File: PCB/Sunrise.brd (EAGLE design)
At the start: 73 x 44 mm, 66 parts, among them IC1 STNS01, IC2 MT2492, J2 B2B-PH-K-S, J3 POWER_JACK, M1 E73-2G4M04S, Q1 IRLHM630, Q2 IRLHM630, Q3 IRLHM630

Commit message: PCB: Clean schematic, move values on board around a bit, no actual connectivity or component changes
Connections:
- new net SLEEP: M1.29
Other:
- board text added: "+ G R B"
- board text removed: "+ R G B"

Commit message: PCB: Minor update to NRF52 module; specify a package variant and expand its description
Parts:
- M1: value E73-2G4M04S -> E73-2G4M04S1B
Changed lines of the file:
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@@
 <attribute name="VALUE" x="26" y="18.5" size="0.6" layer="27" font="vector" ratio="15" rot="R180" align="center"/>
 </element>
-<element name="M1" library="E73-2G4M04S" package="E73-2GM404S" value="E73-2G4M04S" x="64.28" y="29.48" smashed="yes">
+<element name="M1" library="E73-2G4M04S" package="E73-2GM404S" value="E73-2G4M04S1B" x="64.28" y="29.48" smashed="yes">
 <attribute name="NAME" x="71.03" y="39.98" size="0.6" layer="25" font="vector" ratio="15" align="center"/>
 <attribute name="VALUE" x="64.28" y="29.48" size="0.6" layer="27" font="vector" ratio="15" align="center"/>

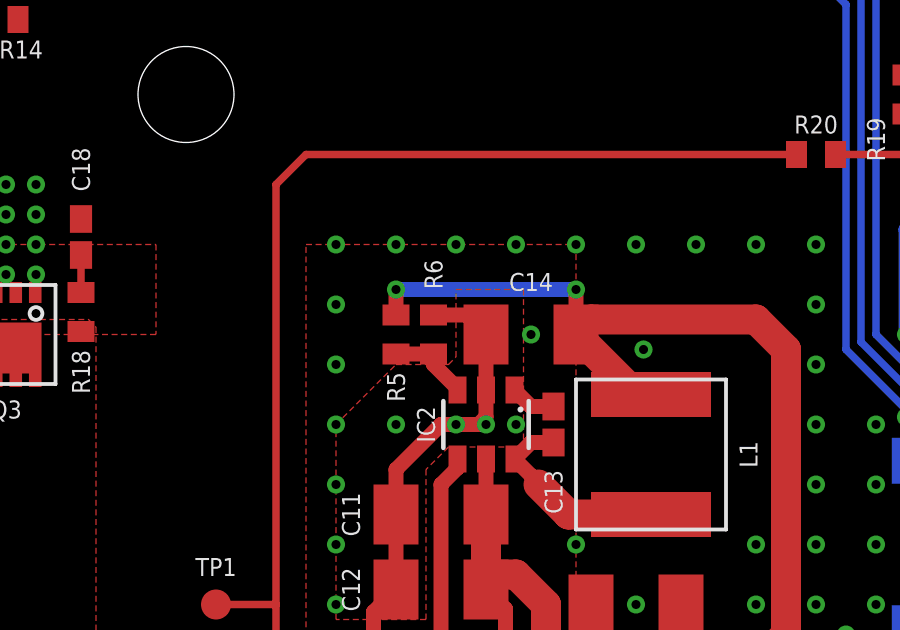
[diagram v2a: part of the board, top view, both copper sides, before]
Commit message: Relabel red/green/blue channels to match common RGB strips
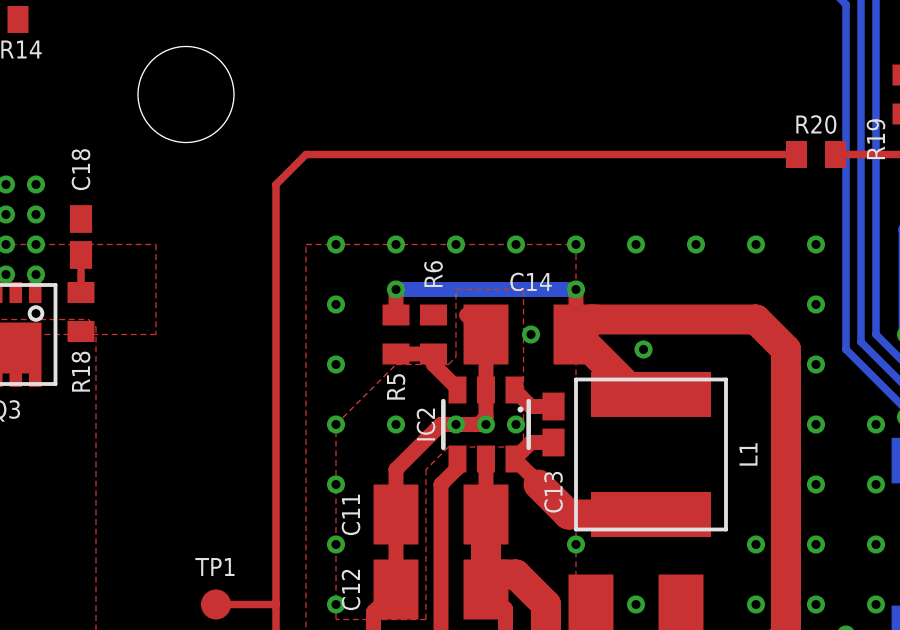
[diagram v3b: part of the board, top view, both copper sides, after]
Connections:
- net BG: now also M1.26, Q3.GATE, R14.2, TP5.TP; no longer M1.28, Q1.GATE, R12.2, TP3.TP
- net GG: now also M1.28, Q1.GATE, R12.2, TP3.TP; no longer M1.27, Q2.GATE, R13.2, TP4.TP
- net RG: now also M1.27, Q2.GATE, R13.2, TP4.TP; no longer M1.26, Q3.GATE, R14.2, TP5.TP
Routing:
- net BG: track 79.9 -> 65.0 mm
- net GG: track 71.5 -> 79.9 mm
- net RG: track 65.0 -> 71.5 mm
- net GND: track 14.8 -> 13.7 mm
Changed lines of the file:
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@@
 <setting verticaltext="up"/>
 </settings>
-<grid distance="0.25" unitdist="mm" unit="mm" style="lines" multiple="8" display="no" altdistance="0.025" altunitdist="inch" altunit="inch"/>
+<grid distance="0.25" unitdist="mm" unit="mm" style="lines" multiple="4" display="yes" altdistance="0.025" altunitdist="inch" altunit="inch"/>
 <layers>
 <layer number="1" name="Top" color="4" fill="1" visible="yes" active="yes"/>
@@
 <layer number="20" name="Dimension" color="15" fill="1" visible="yes" active="yes"/>
 <layer number="21" name="tPlace" color="7" fill="1" visible="yes" active="yes"/>
-<layer number="22" name="bPlace" color="7" fill="1" visible="no" active="yes"/>
+<layer number="22" name="bPlace" color="7" fill="1" visible="yes" active="yes"/>
 <layer number="23" name="tOrigins" color="15" fill="1" visible="yes" active="yes"/>
-<layer number="24" name="bOrigins" color="15" fill="1" visible="no" active="yes"/>
+<layer number="24" name="bOrigins" color="15" fill="1" visible="yes" active="yes"/>
 <layer number="25" name="tNames" color="7" fill="1" visible="yes" active="yes"/>
-<layer number="26" name="bNames" color="7" fill="1" visible="no" active="yes"/>
-<layer number="27" name="tValues" color="10" fill="1" visible="no" active="yes"/>
+<layer number="26" name="bNames" color="7" fill="1" visible="yes" active="yes"/>
+<layer number="27" name="tValues" color="23" fill="1" visible="no" active="yes"/>
 <layer number="28" name="bValues" color="7" fill="1" visible="no" active="yes"/>
 <layer number="29" name="tStop" color="7" fill="3" visible="yes" active="yes"/>
-<layer number="30" name="bStop" color="7" fill="6" visible="no" active="yes"/>
+<layer number="30" name="bStop" color="7" fill="6" visible="yes" active="yes"/>
 <layer number="31" name="tCream" color="7" fill="4" visible="no" active="yes"/>
 <layer number="32" name="bCream" color="7" fill="5" visible="no" active="yes"/>
@@
 <layer number="50" name="dxf" color="7" fill="1" visible="no" active="no"/>
 <layer number="51" name="tDocu" color="7" fill="1" visible="yes" active="yes"/>
-<layer number="52" name="bDocu" color="7" fill="1" visible="no" active="yes"/>
+<layer number="52" name="bDocu" color="7" fill="1" visible="yes" active="yes"/>
 <layer number="53" name="tGND_GNDA" color="7" fill="9" visible="no" active="no"/>
 <layer number="54" name="bGND_GNDA" color="1" fill="9" visible="no" active="no"/>
@@
 <contactref element="R9" pad="1"/>
 <wire x1="29" y1="27.15" x2="29" y2="29" width="0.5" layer="1"/>
-<wire x1="27.25" y1="29.65" x2="28.35" y2="29.65" width="0.5" layer="1"/>
 <wire x1="28.35" y1="29.65" x2="29" y2="29" width="0.5" layer="1"/>
 <wire x1="26" y1="20.5" x2="26" y2="23" width="0.5" layer="1"/>
@@
 <vertex x="48" y="16"/>
 </polygon>
-<polygon width="0.25" layer="1" spacing="0.2" thermals="no" rank="6">
+<polygon width="0.25" layer="1" spacing="0.2" rank="6">
 <vertex x="32" y="32"/>
 <vertex x="32" y="17"/>
@@
 <wire x1="32.65" y1="19.85" x2="32.5" y2="20" width="0.5" layer="1"/>
 </signal>
-<signal name="RG">
+<signal name="BG">
 <contactref element="M1" pad="26"/>
 <contactref element="Q3" pad="GATE"/>
@@
 <contactref element="TP5" pad="TP"/>
 </signal>
-<signal name="GG">
+<signal name="RG">
 <contactref element="M1" pad="27"/>
 <contactref element="Q2" pad="GATE"/>
@@
 <contactref element="TP4" pad="TP"/>
 </signal>
-<signal name="BG">
+<signal name="GG">
 <contactref element="M1" pad="28"/>
 <contactref element="Q1" pad="GATE"/>

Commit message: Update some footprints, add attributes to several components
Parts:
- C10, C19, C6, C7, C8, C9: value 2.2uF -> 2u2 X7R
- C11, C12, C15: value 10uF 25v -> 10uF X7R
- C14: value 22uF 10v -> 22uF X7R
- C3: value 1uF -> 1uF X7R
- R16, R17, R18: value 10 -> 10R
- R24: value 100 -> 100R
- moved R7 0.50 mm to (28.5, 18.5)
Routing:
- net +3V3: track 103.3 -> 104.0 mm
